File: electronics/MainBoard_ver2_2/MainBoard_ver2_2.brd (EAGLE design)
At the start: 120 x 70 mm, 76 parts, among them IC1 LTC1480, IC2 LTC1480, IC3 LTC1480, IC4 LTC1480, IC5 LTC4412, M1 FT4232H_MINI_MODULE, Q1 SQM40P10-40L_GE3, Q2 SQM40P10-40L_GE3, Q3 SQM40P10-40L_GE3, Q4 SQM40P10-40L_GE3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

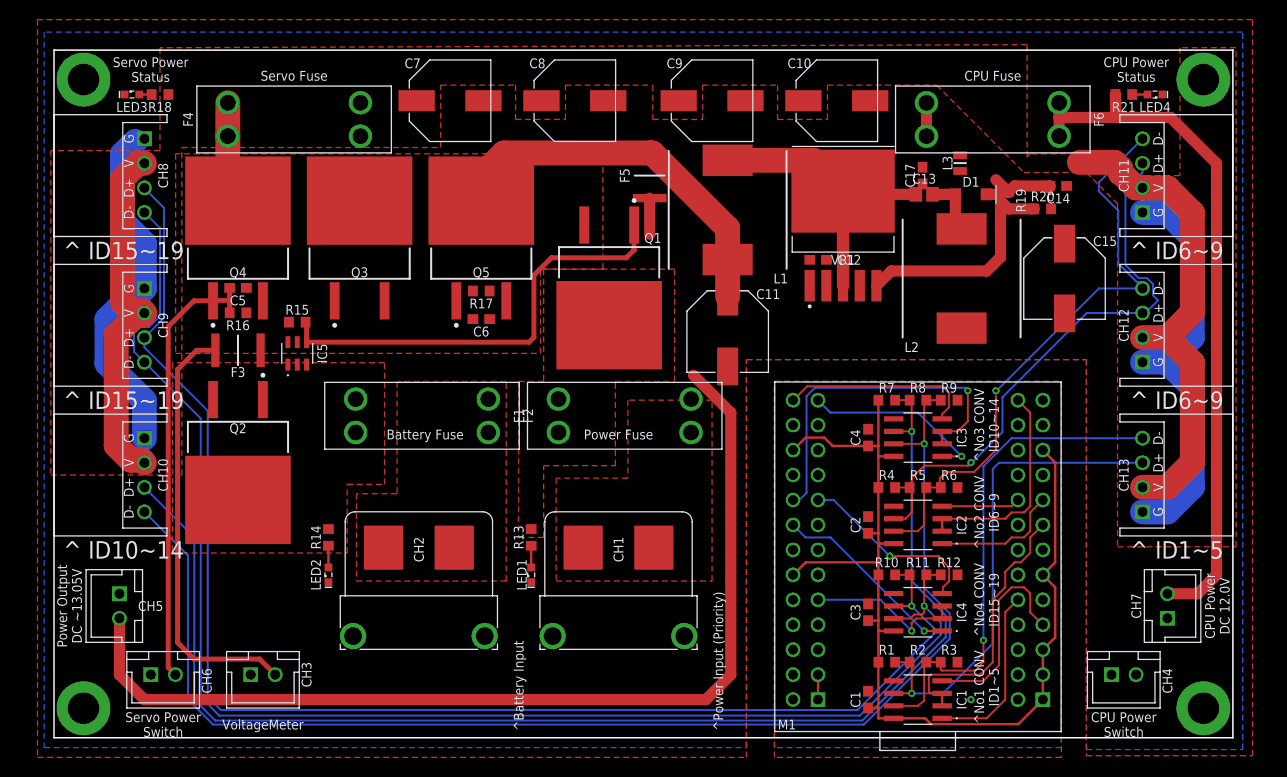
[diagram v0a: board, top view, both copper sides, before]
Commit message: Update MainBoard ver2.2
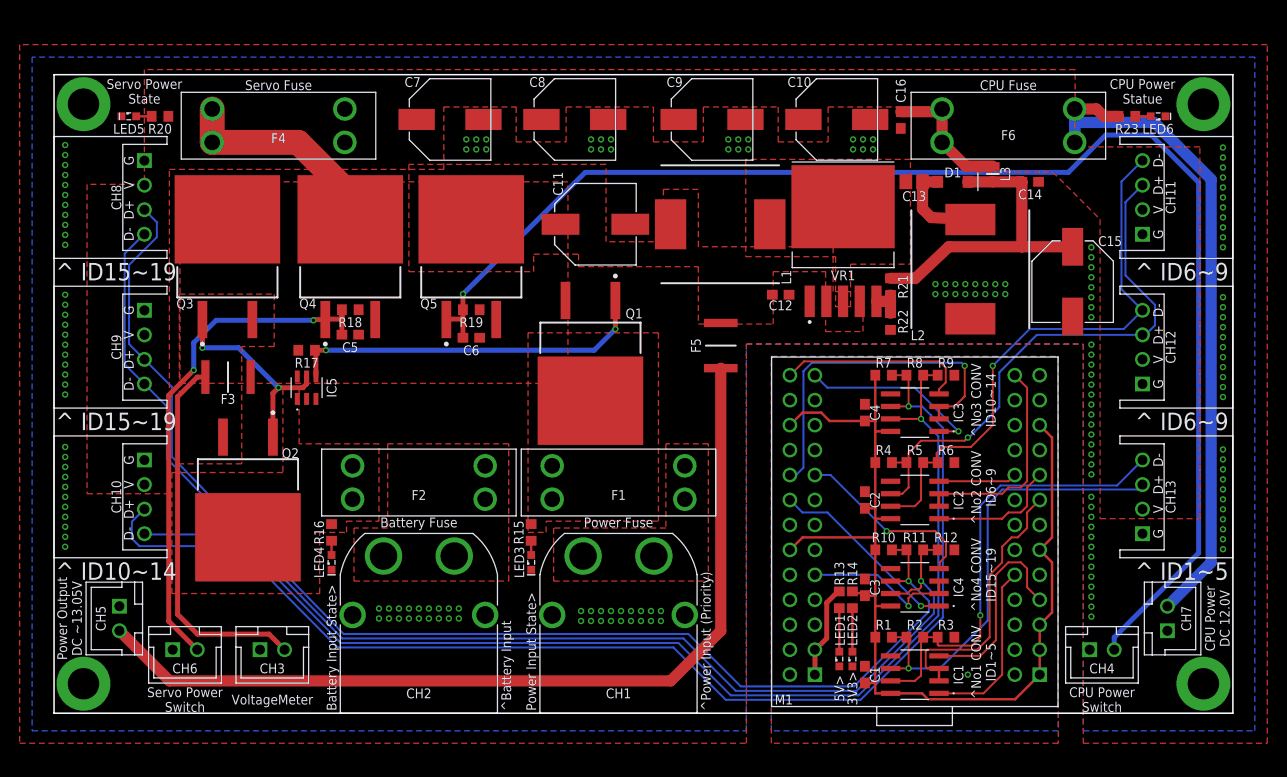
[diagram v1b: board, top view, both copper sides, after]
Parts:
- removed C17: 10u, rcl:C0603
- added C16: 10u, rcl:C0603
- added LED5, LED6: (no value), led:SML0603
- added R22: 1k, rcl:R0603
- added R23: 2k, rcl:R0603
- CH1, CH2: value XT60PT-M -> XT60PW-M; device AMASS_XT60:XT60PT-M -> AMASS_XT60:XT60PW-M
- IC1, IC2, IC3, IC4: value LTC1480 -> ADM3078E; device LTC1480:LTC1480 -> ADM3078E:ADM3078E
- R13, R14: value 2k -> 1k
- R15: value 470k -> 2k
- R16: value 10k -> 2k
- R17: value 10k -> 470k
- R18: value 2k -> 10k
- R19: value 8.66k -> 10k
- R20: value 1k -> 2k
- R21: value 2k -> 8.66k
- moved LED4 96.4 mm to (-31.8, -17.1), turned to 90 degrees
- moved R20 90.3 mm to (-49.2, 28.3), turned to 0 degrees
- moved LED3 62.6 mm to (-11.4, -17.1), turned to 90 degrees
- moved R19 55.8 mm to (-17.5, 8.57), turned to 0 degrees
- moved LED2 54.0 mm to (21.3, -27.0)
- moved R14 53.7 mm to (21.3, -21.0)
- moved LED1 32.5 mm to (19.9, -27.0)
- moved R15 32.0 mm to (-11.4, -14.1), turned to 90 degrees
- moved R13 32.0 mm to (19.9, -21.0)
- moved R21 30.8 mm to (25.1, 10.9), turned to 90 degrees
- moved R18 29.2 mm to (-29.8, 8.57)
- moved R16 24.3 mm to (-31.8, -14.1), turned to 90 degrees
- moved R17 18.8 mm to (-34.3, 4.45), turned to 180 degrees
- moved F5 18.8 mm to (7.87, 4.92)
- moved C11 17.3 mm to (-4.89, 17.3), turned to 0 degrees
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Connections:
- removed net VBUS_TO_VCC: M1.CN3-1, M1.CN3-3
- new net +UB: M1.CN3-1, M1.CN3-3, R13.2
- new net LED_3V3: LED2.A, R14.1
- new net LED_UB: LED1.A, R13.1
- net +3V3: now also R14.2
- net AGND: now also LED1.C, LED2.C
- net A_DIODE_DCDC: now also R21.2; no longer R19.2
- net A_FUSE_BATT: now also R16.2; no longer R14.2
- net A_FUSE_DCDC: now also R23.2; no longer R21.2
- net A_FUSE_PWR: now also R15.2; no longer R13.2
- net A_FUSE_SERVO: now also R20.2; no longer R18.2
- net B_FUSE_DCDC: now also C16.1; no longer C17.1
- net B_LOAD_CPU: now also R19.1; no longer R17.1
- net B_LOAD_SERVO: now also R18.1; no longer R16.1
- net FB_DCDC: now also R21.1, R22.2; no longer R19.1, R20.2
- net GND: now also C16.2, LED5.C, LED6.C, R22.1; no longer C17.2, LED1.C, LED2.C, R20.1
- net INPUT_PWR: now also R18.2, R19.2; no longer R15.2, R16.2
- net LED_BATT: now also LED4.A, R16.1; no longer LED2.A, R14.1
- net LED_DCDCOUT: now also LED6.A, R23.1; no longer LED4.A, R21.1
- net LED_PWR: now also LED3.A, R15.1; no longer LED1.A, R13.1
- net LED_SERVO: now also LED5.A, R20.1; no longer LED3.A, R18.1
- net LTC4412_STAT: now also R17.1; no longer R15.1
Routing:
- net B_LOAD_CPU: track 0.00 -> 140.9 mm, vias 0 -> 1
- net A_FUSE_SERVO: track 87.4 -> 0.00 mm
- net GND: track 77.6 -> 0.00 mm, vias 0 -> 177
- net CPU_PWR_IN: track 42.3 -> 0.00 mm
- net SW_DCDC: track 34.2 -> 0.00 mm
- net A_DIODE_DCDC: track 8.88 -> 32.2 mm
- net LTC4412_GATE: track 0.00 -> 21.7 mm, vias 0 -> 2
- net FB_DCDC: track 22.8 -> 3.29 mm
- net RS485_NO4_D-: track 146.3 -> 129.3 mm
- net RS485_NO4_D+: track 144.2 -> 129.2 mm
- net POWER_OUTPUT: track 105.8 -> 92.2 mm
- net B_FUSE_SERVO: track 12.1 -> 24.8 mm
- net RS485_NO3_D-: track 133.2 -> 120.9 mm
- net B_FUSE_DCDC: track 3.40 -> 13.9 mm
- net +UB: track 0.00 -> 9.64 mm
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- added copper zone on layer 1, net CPU_PWR_IN
- added copper zone on layer 1, net SOURCE
- added copper zone on layer 1, net SW_DCDC
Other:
- board size 120 x 70 mm -> 120 x 65 mm
- board text added: "3V3>"
- board text added: "5V>"
- board text added: "Battery Input State>"
- board text added: "CPU Power Statue"
- board text added: "Power Input State>"
- board text added: "RoboCup Soccer Humanoid Team CIT Brains http://www.cit-brains.net/ SUSTAINA MainBoard Ver2.2 Designed by Masato Kubotera on April 10, 2022."
- board text added: "Servo Power State"
- board text removed: "CPU Power Status"
- board text removed: "RoboCup Soccer Humanoid Team CIT Brains http://www.cit-brains.net/ GankenKun MainBoard Ver2.2 Designed by Masato Kubotera on April 5, 2022."
- board text removed: "Servo 1"
- board text removed: "Servo 2"
- board text removed: "Servo 3"
- board text removed: "Servo 4"
- board text removed: "Servo 5"
- board text removed: "Servo 6"
- board text removed: "Servo Power Status"
